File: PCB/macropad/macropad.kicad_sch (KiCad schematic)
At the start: 13 parts, among them SW1 SW_Push, SW10 SW_Push, SW11 SW_Push, SW12 RotaryEncoder_Switch, SW2 SW_Push, SW3 SW_Push, SW4 SW_Push, SW5 SW_Push, SW6 SW_Push, SW7 SW_Push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

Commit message: Created Basic Schematic and PCB
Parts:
- removed SW1, SW10, SW11, SW2, SW3, SW4, SW5, SW6, SW7, SW8, SW9: SW_Push, symbol Switch:SW_Push
- added D1, D10, D11, D12, D2, D3, D4, D5, D6, D7, D8, D9: 1N4148, Diode_THT:D_DO-35_SOD27_P7.62mm_Horizontal, symbol Diode:1N4148
- added J1: Conn_01x04, footprints:SSD1306-0.91-OLED-4pin-128x32, symbol Connector_Generic:Conn_01x04
- added SW1, SW10, SW11, SW2, SW3, SW4, SW5, SW6, SW7, SW8, SW9: SW_Push_45deg, Button_Switch_Keyboard:SW_Cherry_MX_1.00u_PCB, symbol Switch:SW_Push_45deg
- SW12: footprint (none) -> Rotary_Encoder:RotaryEncoder_Alps_EC11E-Switch_Vertical_H20mm
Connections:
- net GND: now also SW12.C, J1.1 (Pin_1)
- net EC11A: now reaches SW12.A
- net EC11A: now also U1.9 (PA7_A8_D8_SCK)
- net EC11B: now reaches SW12.B
- net EC11B: now also U1.8 (PB09_A7_D7_RX)
- net Col 2: now reaches SW12.S1
- net Col 2: now also U1.3 (PA10_A2_D2), SW10.1, SW11.1, SW9.1
- net EC11SWA: now reaches SW12.S2
- net EC11SWA: now also D12.2 (A)
- net Col 0: now reaches U1.1 (PA02_A0_D0)
- net Col 0: now also SW1.1, SW2.1, SW3.1, SW4.1
- net Row 2: now reaches U1.10 (PA5_A9_D9_MISO)
- net Row 2: now also D10.1 (K), D3.1 (K), D7.1 (K)
- net Row 3: now reaches U1.11 (PA6_A10_D10_MOSI)
- net Row 3: now also D11.1 (K), D4.1 (K), D8.1 (K)
- net VCC: now reaches U1.12 (3V3)
- net VCC: now also J1.2 (Pin_2)
- net Col 1: now reaches U1.2 (PA4_A1_D1)
- net Col 1: now also SW5.1, SW6.1, SW7.1, SW8.1
- net Row 0: now reaches U1.4 (PA11_A3_D3)
- net Row 0: now also D1.1 (K), D12.1 (K), D5.1 (K)
- net SDA: now reaches U1.5 (PA8_A4_D4_SDA)
- net SDA: now also J1.4 (Pin_4)
- net SCL: now reaches U1.6 (PA9_A5_D5_SCL)
- net SCL: now also J1.3 (Pin_3)
- net Row 1: now reaches U1.7 (PB08_A6_D6_TX)
- net Row 1: now also D2.1 (K), D6.1 (K), D9.1 (K)
- new net: D4.2 (A), SW4.2
- new net: D2.2 (A), SW2.2
- new net: D6.2 (A), SW6.2
- new net: D5.2 (A), SW5.2
- new net: D1.2 (A), SW1.2
- new net: D8.2 (A), SW8.2
- new net: D10.2 (A), SW10.2
- new net: D7.2 (A), SW7.2
- new net: D3.2 (A), SW3.2
- new net: D11.2 (A), SW11.2
- new net: D9.2 (A), SW9.2
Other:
- moved on the sheet: SW12

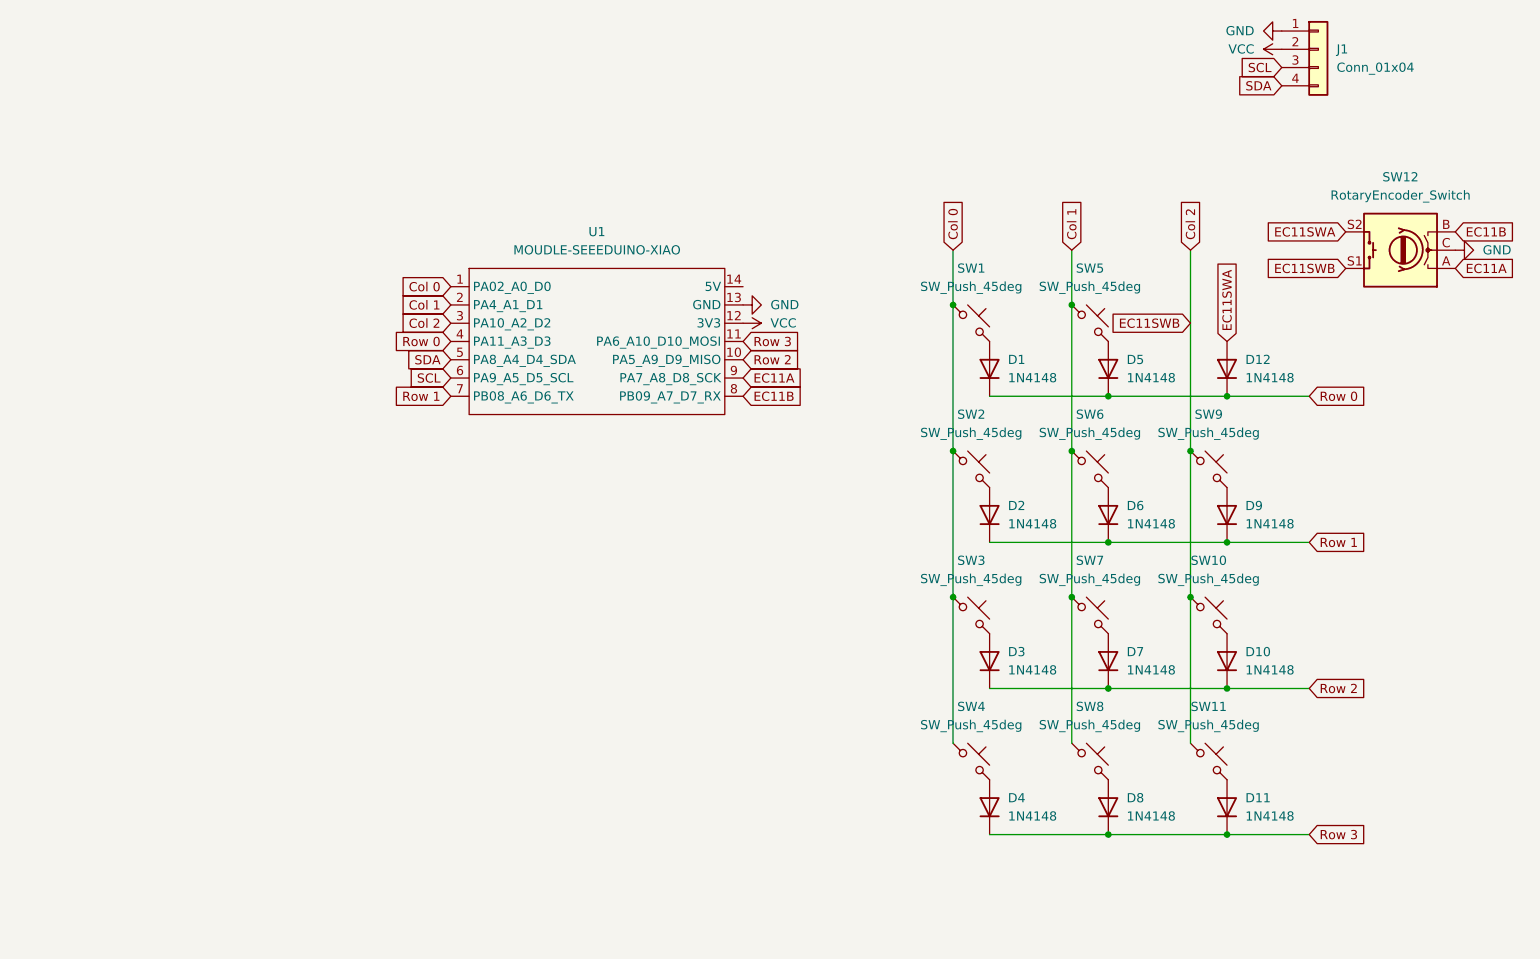
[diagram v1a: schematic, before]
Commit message: Wired components together on PCB
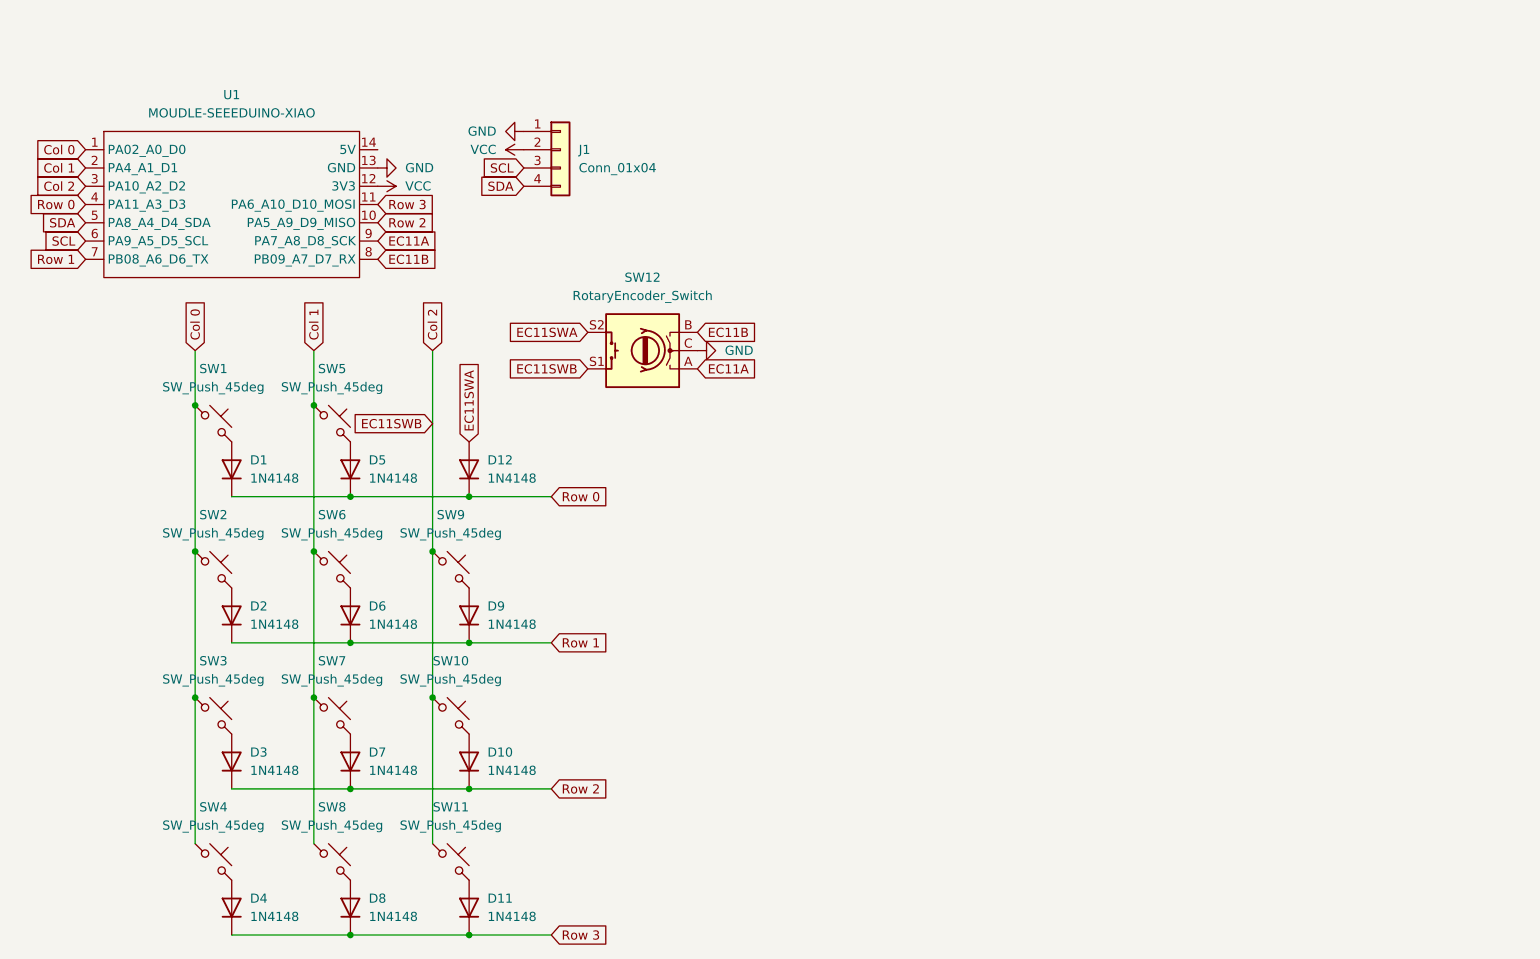
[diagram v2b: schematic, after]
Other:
- moved on the sheet: D1, D10, D11, D12, D2, D3, D4, D5, D6, D7, D8, D9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
